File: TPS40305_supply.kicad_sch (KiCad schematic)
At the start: 20 parts

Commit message: added the jellybean footprints
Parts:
- added C? (x2): 47uF, Capacitor_SMD:C_1210_3225Metric, symbol Device:C
- C1: renamed from C?; footprint (none) -> Capacitor_SMD:C_1210_3225Metric; DK (none) -> 490-6539-1-ND; PARTNO (none) -> GRM32ER61C476KE15L
- C10: renamed from C?; footprint (none) -> Capacitor_SMD:C_1206_3216Metric
- C2, C3, C5, C7, C8: renamed from C?; footprint (none) -> Capacitor_SMD:C_0805_2012Metric
- C4, C6: renamed from C?; footprint (none) -> Capacitor_SMD:C_0402_1005Metric
- C9: renamed from C?; DK (none) -> P16200CT-ND; PARTNO (none) -> 2R5TPE220MAFB
- L1: renamed from L?; value L -> 150nH; DK (none) -> 513-1568-1-ND; PARTNO (none) -> FP1005R1-R15-R
- R1, R2, R3, R4, R5, R6: renamed from R?; footprint (none) -> Resistor_SMD:R_0402_1005Metric
- gave numbers to parts that had none: 3
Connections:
- net GND: now also C?.2, C?.2
- net VIN: now also C?.1, C?.1
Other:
- moved on the sheet: C3, R2

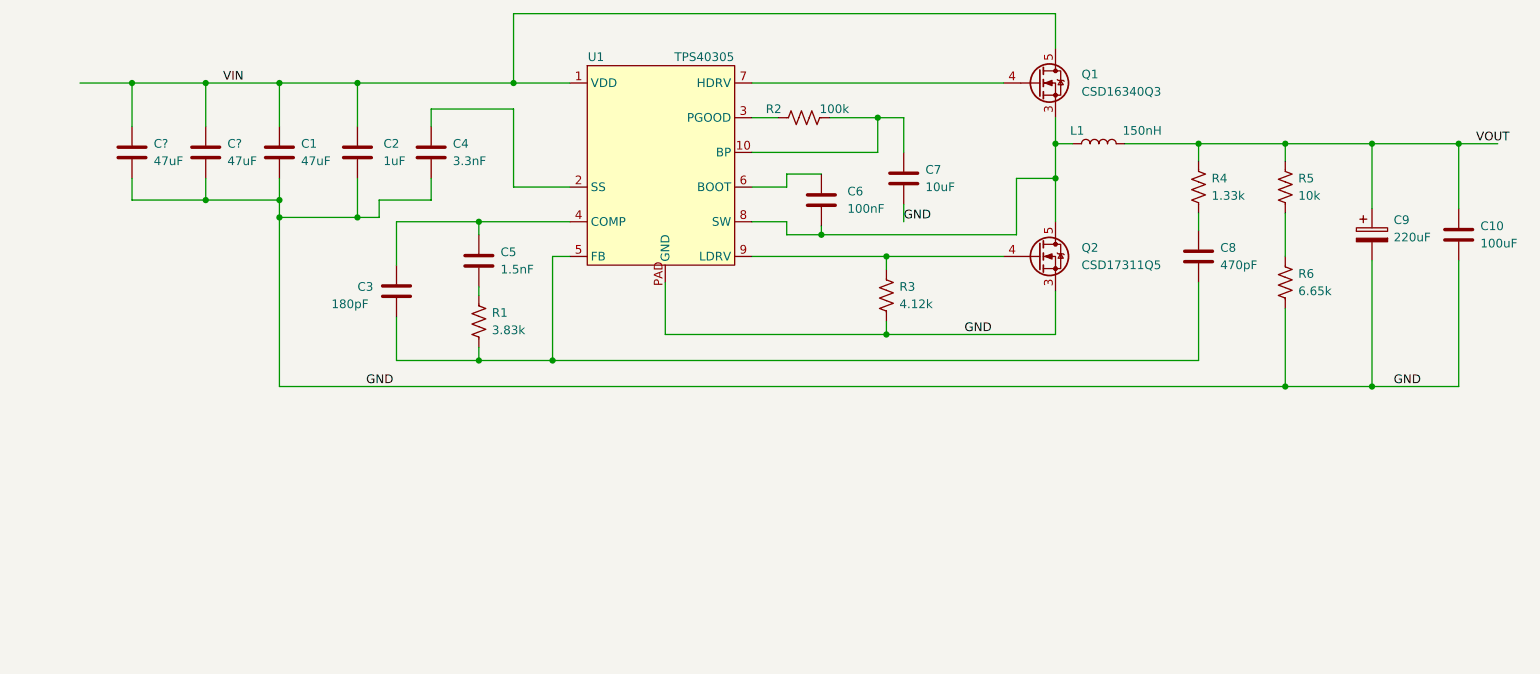
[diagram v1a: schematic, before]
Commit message: started on some of the mosfet footprints
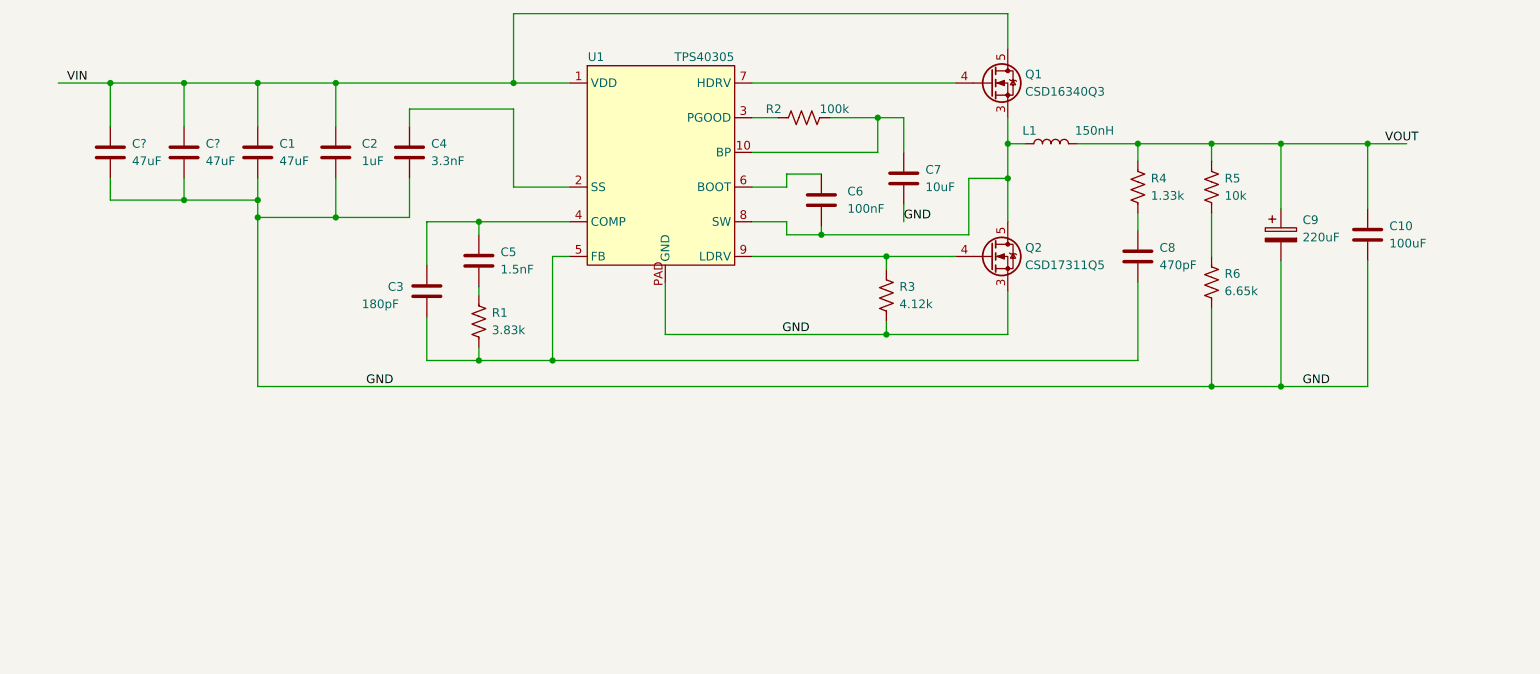
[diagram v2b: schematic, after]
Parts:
- C10: DK (none) -> 445-6008-1-ND; PARTNO (none) -> C3216X5R0J107M160AB
- Q2: footprint (none) -> TPS40305_supply:CSD17311Q5
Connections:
- net at C6.2, L1.1, Q1.1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: no longer Q2.6, Q2.7, Q2.8
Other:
- moved on the sheet: C1, C10, C2, C3, C4, C8, C9, C?, L1, Q1, Q2, R4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

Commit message: added footprints
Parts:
- added R7: 2k, TPS40305_supply:ST4ETB202, symbol Device:R_Potentiometer_US
- C11: renamed from C9; footprint (none) -> TPS40305_supply:CAP_2R5TPE220MAFB
- L1: footprint (none) -> TPS40305_supply:FP1005R1-R15-R
- Q1: footprint (none) -> TPS40305_supply:CSD16340Q3
- R6: value 6.65k -> 5.62k
- U1: footprint (none) -> TPS40305_supply:TPS40305; DK (none) -> 296-25487-1-ND; PARTNO (none) -> TPS40305DRCT
- gave numbers to parts that had none: 2
- renumbered C8 to C10, C10 to C12, C1 to C3, C2 to C4, C4 to C5, C3 to C6, C5 to C7, C6 to C8, C7 to C9
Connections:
- net GND: now also U1.11 (GND), R7.1; no longer R6.2, U1.PAD (GND)
- net VIN: no longer Q1.6, Q1.7, Q1.8
- net at R5.2, R6.1: now also C10.2, C6.2, R1.2, U1.5 (FB)
- new net: R6.2, R7.2
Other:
- moved on the sheet: R5, R6

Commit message: added spade connectors ("we need a spade if we're gonna dig a pit.")
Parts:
- added J1, J2, J3, J4: Conn_01x01, TPS40305_supply:63862-1, symbol Connector_Generic:Conn_01x01
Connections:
- net GND: now also J2.1 (Pin_1), J4.1 (Pin_1)
- net VIN: now also J1.1 (Pin_1)
- net VOUT: now also J3.1 (Pin_1)
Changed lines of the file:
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@@
   (junction (at 60.96 87.63) (diameter 0) (color 0 0 0 0)
   )
+  (junction (at 60.96 104.775) (diameter 0) (color 0 0 0 0)
+  )
   (junction (at 82.55 104.775) (diameter 0) (color 0 0 0 0)
   )
+  (junction (at 245.11 132.08) (diameter 0) (color 0 0 0 0)
+  )
   (junction (at 125.73 128.27) (diameter 0) (color 0 0 0 0)
   )
@@
   (junction (at 213.995 135.89) (diameter 0) (color 0 0 0 0)
   )
+  (wire (pts (xy 245.11 113.665) (xy 245.11 132.08))
+    (stroke (width 0) (type default) (color 0 0 0 0))
+  )
   (wire (pts (xy 114.935 107.95) (xy 107.315 107.95))
     (stroke (width 0) (type default) (color 0 0 0 0))
@@
     (stroke (width 0) (type default) (color 0 0 0 0))
   )
-  (wire (pts (xy 245.11 96.52) (xy 250.825 96.52))
+  (wire (pts (xy 254.635 102.87) (xy 255.905 102.87))
+    (stroke (width 0) (type default) (color 0 0 0 0))
+  )
+  (wire (pts (xy 245.11 96.52) (xy 255.905 96.52))
     (stroke (width 0) (type default) (color 0 0 0 0))
   )
@@
     (stroke (width 0) (type default) (color 0 0 0 0))
   )
+  (wire (pts (xy 254.635 102.87) (xy 254.635 132.08))
+    (stroke (width 0) (type default) (color 0 0 0 0))
+  )
   (wire (pts (xy 125.73 128.27) (xy 114.935 128.27))
     (stroke (width 0) (type default) (color 0 0 0 0))
   )
+  (wire (pts (xy 53.34 104.775) (xy 60.96 104.775))
+    (stroke (width 0) (type default) (color 0 0 0 0))
+  )
   (wire (pts (xy 104.775 101.6) (xy 104.775 107.315))
     (stroke (width 0) (type default) (color 0 0 0 0))
@@
     (stroke (width 0) (type default) (color 0 0 0 0))
   )
+  (wire (pts (xy 53.34 93.345) (xy 53.34 104.775))
+    (stroke (width 0) (type default) (color 0 0 0 0))
+  )
   (wire (pts (xy 71.755 87.63) (xy 82.55 87.63))
     (stroke (width 0) (type default) (color 0 0 0 0))
@@
     (stroke (width 0) (type default) (color 0 0 0 0))
   )
-  (wire (pts (xy 245.11 113.665) (xy 245.11 132.08))
-    (stroke (width 0) (type default) (color 0 0 0 0))
-  )
   (wire (pts (xy 174.625 124.46) (xy 174.625 122.555))
     (stroke (width 0) (type default) (color 0 0 0 0))
@@
   )
   (wire (pts (xy 114.935 126.365) (xy 114.935 128.27))
+    (stroke (width 0) (type default) (color 0 0 0 0))
+  )
+  (wire (pts (xy 254.635 132.08) (xy 245.11 132.08))
     (stroke (width 0) (type default) (color 0 0 0 0))
   )
@@
     (pin "1")
     (pin "2")
+  )
+  (symbol (lib_id "Connector_Generic:Conn_01x01") (at 260.985 102.87 0) (unit 1)
+    (in_bom yes) (on_board yes)
+    (property "Reference" "J4" (id 0) (at 260.985 100.33 0))
+    (property "Value" "Conn_01x01" (id 1) (at 260.985 106.68 0)
+      (effects (font (size 1.27 1.27)) hide)
+    )
+    (property "Footprint" "TPS40305_supply:63862-1" (id 2) (at 260.985 102.87 0)
+      (effects (font (size 1.27 1.27)) hide)
+    )
+    (property "Datasheet" "https://www.te.com/commerce/DocumentDelivery/DDEController?Action=srchrtrv&DocNm=63862&DocType=Customer+Drawing&DocLang=English" (id 3) (at 260.985 102.87 0)
+      (effects (font (size 1.27 1.27)) hide)
+    )
+    (property "DK" "A100886CT-ND" (id 4) (at 260.985 102.87 0)
+      (effects (font (size 1.27 1.27)) hide)
+    )
+    (property "PARTNO" "63862-1" (id 5) (at 260.985 102.87 0)
+      (effects (font (size 1.27 1.27)) hide)
+    )
+    (pin "1")
   )
   (symbol (lib_name "Q_NMOS_CSD17311Q5_1") (lib_id "TPS40305:Q_NMOS_CSD17311Q5") (at 189.865 113.03 0) (unit 1)
@@
     (pin "2")
   )
+  (symbol (lib_id "Connector_Generic:Conn_01x01") (at 48.26 87.63 180) (unit 1)
+    (in_bom yes) (on_board yes)
+    (property "Reference" "J1" (id 0) (at 48.26 85.09 0))
+    (property "Value" "Conn_01x01" (id 1) (at 48.26 83.82 0)
+      (effects (font (size 1.27 1.27)) hide)
+    )
+    (property "Footprint" "TPS40305_supply:63862-1" (id 2) (at 48.26 87.63 0)
+      (effects (font (size 1.27 1.27)) hide)
+    )
+    (property "Datasheet" "https://www.te.com/commerce/DocumentDelivery/DDEController?Action=srchrtrv&DocNm=63862&DocType=Customer+Drawing&DocLang=English" (id 3) (at 48.26 87.63 0)
+      (effects (font (size 1.27 1.27)) hide)
+    )
+    (property "DK" "A100886CT-ND" (id 4) (at 48.26 87.63 0)
+      (effects (font (size 1.27 1.27)) hide)
+    )
+    (property "PARTNO" "63862-1" (id 5) (at 48.26 87.63 0)
+      (effects (font (size 1.27 1.27)) hide)
+    )
+    (pin "1")
+  )
   (symbol (lib_id "Device:R_Potentiometer_US") (at 222.25 135.89 90) (unit 1)
     (in_bom yes) (on_board yes) (fields_autoplaced)
@@
     (pin "2")
   )
+  (symbol (lib_id "Connector_Generic:Conn_01x01") (at 48.26 93.345 180) (unit 1)
+    (in_bom yes) (on_board yes)
+    (property "Reference" "J2" (id 0) (at 48.26 90.805 0))
+    (property "Value" "Conn_01x01" (id 1) (at 48.26 89.535 0)
+      (effects (font (size 1.27 1.27)) hide)
+    )
+    (property "Footprint" "TPS40305_supply:63862-1" (id 2) (at 48.26 93.345 0)
+      (effects (font (size 1.27 1.27)) hide)
+    )
+    (property "Datasheet" "https://www.te.com/commerce/DocumentDelivery/DDEController?Action=srchrtrv&DocNm=63862&DocType=Customer+Drawing&DocLang=English" (id 3) (at 48.26 93.345 0)
+      (effects (font (size 1.27 1.27)) hide)
+    )
+    (property "DK" "A100886CT-ND" (id 4) (at 48.26 93.345 0)
+      (effects (font (size 1.27 1.27)) hide)
+    )
+    (property "PARTNO" "63862-1" (id 5) (at 48.26 93.345 0)
+      (effects (font (size 1.27 1.27)) hide)
+    )
+    (pin "1")
+  )
   (symbol (lib_id "Device:R_US") (at 162.56 92.71 90) (unit 1)
     (in_bom yes) (on_board yes)
@@
     (pin "1")
     (pin "2")
+  )
+  (symbol (lib_id "Connector_Generic:Conn_01x01") (at 260.985 96.52 0) (unit 1)
+    (in_bom yes) (on_board yes)
+    (property "Reference" "J3" (id 0) (at 260.985 93.98 0))
+    (property "Value" "Conn_01x01" (id 1) (at 260.985 100.33 0)
+      (effects (font (size 1.27 1.27)) hide)
+    )
+    (property "Footprint" "TPS40305_supply:63862-1" (id 2) (at 260.985 96.52 0)
+      (effects (font (size 1.27 1.27)) hide)
+    )
+    (property "Datasheet" "https://www.te.com/commerce/DocumentDelivery/DDEController?Action=srchrtrv&DocNm=63862&DocType=Customer+Drawing&DocLang=English" (id 3) (at 260.985 96.52 0)
+      (effects (font (size 1.27 1.27)) hide)
+    )
+    (property "DK" "A100886CT-ND" (id 4) (at 260.985 96.52 0)
+      (effects (font (size 1.27 1.27)) hide)
+    )
+    (property "PARTNO" "63862-1" (id 5) (at 260.985 96.52 0)
+      (effects (font (size 1.27 1.27)) hide)
+    )
+    (pin "1")
   )
   (symbol (lib_id "Device:C") (at 82.55 97.79 0) (unit 1)
@@
       (reference "C12") (unit 1) (value "100uF") (footprint "Capacitor_SMD:C_1206_3216Metric")
     )
+    (path "/17bed92d-5fb8-4e75-bb9f-233d3b0ecbed"
+      (reference "J1") (unit 1) (value "Conn_01x01") (footprint "TPS40305_supply:63862-1")
+    )
+    (path "/607146e7-6c98-4f12-83f2-bf57c1282bbb"
+      (reference "J2") (unit 1) (value "Conn_01x01") (footprint "TPS40305_supply:63862-1")
+    )
+    (path "/d24a5004-c2e3-458d-bf8d-1814c28f789b"
+      (reference "J3") (unit 1) (value "Conn_01x01") (footprint "TPS40305_supply:63862-1")
+    )
+    (path "/061dbaf9-ccf9-4c91-826e-caa1f84d31b4"
+      (reference "J4") (unit 1) (value "Conn_01x01") (footprint "TPS40305_supply:63862-1")
+    )
     (path "/874ceeb7-dd09-40c6-a642-cdf6f678305b"

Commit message: more layout
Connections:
- net SW: now reaches C8.2, L1.1, Q1.1, Q1.2, Q1.3 (S), Q2.5 (D), U1.8 (SW)
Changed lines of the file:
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@@
+    (effects (font (size 1.27 1.27)) (justify left bottom))
+  )
+  (label "SW" (at 192.405 101.6 0)
     (effects (font (size 1.27 1.27)) (justify left bottom))
   )

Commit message: added DK part numbers and generated BOM
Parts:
- C10: DK (none) -> 1292-1580-1-ND
- C4: DK (none) -> 1276-6471-1-ND
- C5: DK (none) -> 1276-1552-1-ND
- C6: DK (none) -> 311-1114-1-ND
- C7: DK (none) -> 311-1128-1-ND
- C8: value 100nF -> 0.1uF; DK (none) -> 1276-1043-1-ND
- C9: DK (none) -> 1276-1096-1-ND
- R1: DK (none) -> 311-3.83KLRCT-ND
- R2: DK (none) -> 311-100KJRCT-ND
- R3: DK (none) -> RMCF0402FT4K12CT-ND
- R4: DK (none) -> 311-1.33KLRCT-ND
- R5: DK (none) -> 13-RC0402JR-1310KLTR-ND
- R6: DK (none) -> RMCF0402FT5K62CT-ND
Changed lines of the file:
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@@
       (effects (font (size 1.27 1.27)) (justify left))
     )
-    (property "Value" "100nF" (id 1) (at 168.91 106.0449 0)
+    (property "Value" "0.1uF" (id 1) (at 168.91 106.0449 0)
       (effects (font (size 1.27 1.27)) (justify left))
     )
@@
     )
     (property "Datasheet" "~" (id 3) (at 165.1 104.775 0)
+      (effects (font (size 1.27 1.27)) hide)
+    )
+    (property "DK" "1276-1043-1-ND" (id 4) (at 165.1 104.775 0)
       (effects (font (size 1.27 1.27)) hide)
     )
@@
       (effects (font (size 1.27 1.27)) hide)
     )
+    (property "DK" "RMCF0402FT4K12CT-ND" (id 4) (at 174.625 118.745 0)
+      (effects (font (size 1.27 1.27)) hide)
+    )
     (pin "1")
     (pin "2")
@@
     )
     (property "Datasheet" "~" (id 3) (at 114.935 113.665 0)
+      (effects (font (size 1.27 1.27)) hide)
+    )
+    (property "DK" "311-1128-1-ND" (id 4) (at 114.935 113.665 0)
       (effects (font (size 1.27 1.27)) hide)
     )
@@
       (effects (font (size 1.27 1.27)) hide)
     )
+    (property "DK" "13-RC0402JR-1310KLTR-ND" (id 4) (at 222.25 109.22 0)
+      (effects (font (size 1.27 1.27)) hide)
+    )
     (pin "1")
     (pin "2")
@@
       (effects (font (size 1.27 1.27)) hide)
     )
+    (property "DK" "1276-6471-1-ND" (id 4) (at 93.98 97.79 0)
+      (effects (font (size 1.27 1.27)) hide)
+    )
     (pin "1")
     (pin "2")
@@
       (effects (font (size 1.27 1.27)) hide)
     )
+    (property "DK" "311-3.83KLRCT-ND" (id 4) (at 114.935 122.555 0)
+      (effects (font (size 1.27 1.27)) hide)
+    )
     (pin "1")
     (pin "2")
@@
     )
     (property "Datasheet" "~" (id 3) (at 211.455 102.87 0)
+      (effects (font (size 1.27 1.27)) hide)
+    )
+    (property "DK" "311-1.33KLRCT-ND" (id 4) (at 211.455 102.87 0)
       (effects (font (size 1.27 1.27)) hide)
     )
@@
       (effects (font (size 1.27 1.27)) hide)
     )
+    (property "DK" "311-100KJRCT-ND" (id 4) (at 162.56 92.71 0)
+      (effects (font (size 1.27 1.27)) hide)
+    )
     (pin "1")
     (pin "2")
@@
     )
     (property "Datasheet" "~" (id 3) (at 104.775 97.79 0)
+      (effects (font (size 1.27 1.27)) hide)
+    )
+    (property "DK" "1276-1552-1-ND" (id 4) (at 104.775 97.79 0)
       (effects (font (size 1.27 1.27)) hide)
     )
@@
       (effects (font (size 1.27 1.27)) hide)
     )
+    (property "DK" "1292-1580-1-ND" (id 4) (at 211.455 113.03 0)
+      (effects (font (size 1.27 1.27)) hide)
+    )
     (pin "1")
     (pin "2")
@@
       (effects (font (size 1.27 1.27)) hide)
     )
+    (property "DK" "311-1114-1-ND" (id 4) (at 107.315 118.11 0)
+      (effects (font (size 1.27 1.27)) hide)
+    )
     (pin "1")
     (pin "2")
@@
       (effects (font (size 1.27 1.27)) hide)
     )
-    (property "Datasheet" "~" (id 3) (at 189.865 87.63 0)
+    (property "Datasheet" "https://www.ti.com/lit/ds/symlink/csd16340q3.pdf" (id 3) (at 189.865 87.63 0)
       (effects (font (size 1.27 1.27)) hide)
     )
@@
     )
     (property "Datasheet" "~" (id 3) (at 177.165 101.6 0)
+      (effects (font (size 1.27 1.27)) hide)
+    )
+    (property "DK" "1276-1096-1-ND" (id 4) (at 177.165 101.6 0)
       (effects (font (size 1.27 1.27)) hide)
     )
@@
       (effects (font (size 1.27 1.27)) hide)
     )
+    (property "DK" "RMCF0402FT5K62CT-ND" (id 4) (at 222.25 125.73 0)
+      (effects (font (size 1.27 1.27)) hide)
+    )
     (pin "1")
     (pin "2")
@@
     )
     (path "/019e3fb8-0bfe-44fa-aa6b-fca6c0ff11b9"
-      (reference "C8") (unit 1) (value "100nF") (footprint "Capacitor_SMD:C_0402_1005Metric")
+      (reference "C8") (unit 1) (value "0.1uF") (footprint "Capacitor_SMD:C_0402_1005Metric")
     )
     (path "/b4a0001f-10cb-48d5-9824-ce035b3070d4"

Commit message: added gerbers
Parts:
- added H1, H2, H3, H4: MountingHole, MountingHole:MountingHole_2.2mm_M2, symbol Mechanical:MountingHole
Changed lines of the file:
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@@
     (pin "2")
+  )
+  (symbol (lib_id "Mechanical:MountingHole") (at 106.045 156.21 0) (unit 1)
+    (in_bom yes) (on_board yes) (fields_autoplaced)
+    (property "Reference" "H2" (id 0) (at 109.22 154.9399 0)
+      (effects (font (size 1.27 1.27)) (justify left))
+    )
+    (property "Value" "MountingHole" (id 1) (at 109.22 157.4799 0)
+      (effects (font (size 1.27 1.27)) (justify left))
+    )
+    (property "Footprint" "MountingHole:MountingHole_2.2mm_M2" (id 2) (at 106.045 156.21 0)
+      (effects (font (size 1.27 1.27)) hide)
+    )
+    (property "Datasheet" "~" (id 3) (at 106.045 156.21 0)
+      (effects (font (size 1.27 1.27)) hide)
+    )
   )
   (symbol (lib_id "Device:C") (at 165.1 104.775 0) (unit 1)
@@
     (pin "2")
   )
+  (symbol (lib_id "Mechanical:MountingHole") (at 106.045 163.195 0) (unit 1)
+    (in_bom yes) (on_board yes) (fields_autoplaced)
+    (property "Reference" "H3" (id 0) (at 109.22 161.9249 0)
+      (effects (font (size 1.27 1.27)) (justify left))
+    )
+    (property "Value" "MountingHole" (id 1) (at 109.22 164.4649 0)
+      (effects (font (size 1.27 1.27)) (justify left))
+    )
+    (property "Footprint" "MountingHole:MountingHole_2.2mm_M2" (id 2) (at 106.045 163.195 0)
+      (effects (font (size 1.27 1.27)) hide)
+    )
+    (property "Datasheet" "~" (id 3) (at 106.045 163.195 0)
+      (effects (font (size 1.27 1.27)) hide)
+    )
+  )
   (symbol (lib_id "Connector_Generic:Conn_01x01") (at 48.26 87.63 180) (unit 1)
     (in_bom yes) (on_board yes)
@@
     (pin "3")
   )
+  (symbol (lib_id "Mechanical:MountingHole") (at 106.045 169.545 0) (unit 1)
+    (in_bom yes) (on_board yes) (fields_autoplaced)
+    (property "Reference" "H4" (id 0) (at 109.22 168.2749 0)
+      (effects (font (size 1.27 1.27)) (justify left))
+    )
+    (property "Value" "MountingHole" (id 1) (at 109.22 170.8149 0)
+      (effects (font (size 1.27 1.27)) (justify left))
+    )
+    (property "Footprint" "MountingHole:MountingHole_2.2mm_M2" (id 2) (at 106.045 169.545 0)
+      (effects (font (size 1.27 1.27)) hide)
+    )
+    (property "Datasheet" "~" (id 3) (at 106.045 169.545 0)
+      (effects (font (size 1.27 1.27)) hide)
+    )
+  )
   (symbol (lib_id "Device:R_US") (at 222.25 109.22 0) (unit 1)
     (in_bom yes) (on_board yes) (fields_autoplaced)
@@
     )
     (pin "1")
+  )
+  (symbol (lib_id "Mechanical:MountingHole") (at 106.045 149.86 0) (unit 1)
+    (in_bom yes) (on_board yes) (fields_autoplaced)
+    (property "Reference" "H1" (id 0) (at 109.22 148.5899 0)
+      (effects (font (size 1.27 1.27)) (justify left))
+    )
+    (property "Value" "MountingHole" (id 1) (at 109.22 151.1299 0)
+      (effects (font (size 1.27 1.27)) (justify left))
+    )
+    (property "Footprint" "MountingHole:MountingHole_2.2mm_M2" (id 2) (at 106.045 149.86 0)
+      (effects (font (size 1.27 1.27)) hide)
+    )
+    (property "Datasheet" "~" (id 3) (at 106.045 149.86 0)
+      (effects (font (size 1.27 1.27)) hide)
+    )
   )
   (symbol (lib_id "Device:C") (at 82.55 97.79 0) (unit 1)
@@
       (reference "C12") (unit 1) (value "100uF") (footprint "Capacitor_SMD:C_1206_3216Metric")
     )
+    (path "/d76728d2-d156-4473-aefc-cca4d2525abc"
+      (reference "H1") (unit 1) (value "MountingHole") (footprint "MountingHole:MountingHole_2.2mm_M2")
+    )
+    (path "/008a934d-4b3c-452e-a0f5-f1e33a3b2254"
+      (reference "H2") (unit 1) (value "MountingHole") (footprint "MountingHole:MountingHole_2.2mm_M2")
+    )
+    (path "/139cd192-75fc-4a2a-91a3-caed0b51b815"
+      (reference "H3") (unit 1) (value "MountingHole") (footprint "MountingHole:MountingHole_2.2mm_M2")
+    )
+    (path "/23330a28-8c44-4b78-a6a0-cf5b8493b1ba"
+      (reference "H4") (unit 1) (value "MountingHole") (footprint "MountingHole:MountingHole_2.2mm_M2")
+    )
     (path "/17bed92d-5fb8-4e75-bb9f-233d3b0ecbed"

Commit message: updated busted DK PN
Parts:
- R5: DK 13-RC0402JR-1310KLTR-ND -> 311-10KJRCT-ND
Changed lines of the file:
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@@
       (effects (font (size 1.27 1.27)) hide)
     )
-    (property "DK" "13-RC0402JR-1310KLTR-ND" (id 4) (at 222.25 109.22 0)
+    (property "DK" "311-10KJRCT-ND" (id 4) (at 222.25 109.22 0)
       (effects (font (size 1.27 1.27)) hide)
     )
